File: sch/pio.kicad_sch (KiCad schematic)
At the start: 4 parts

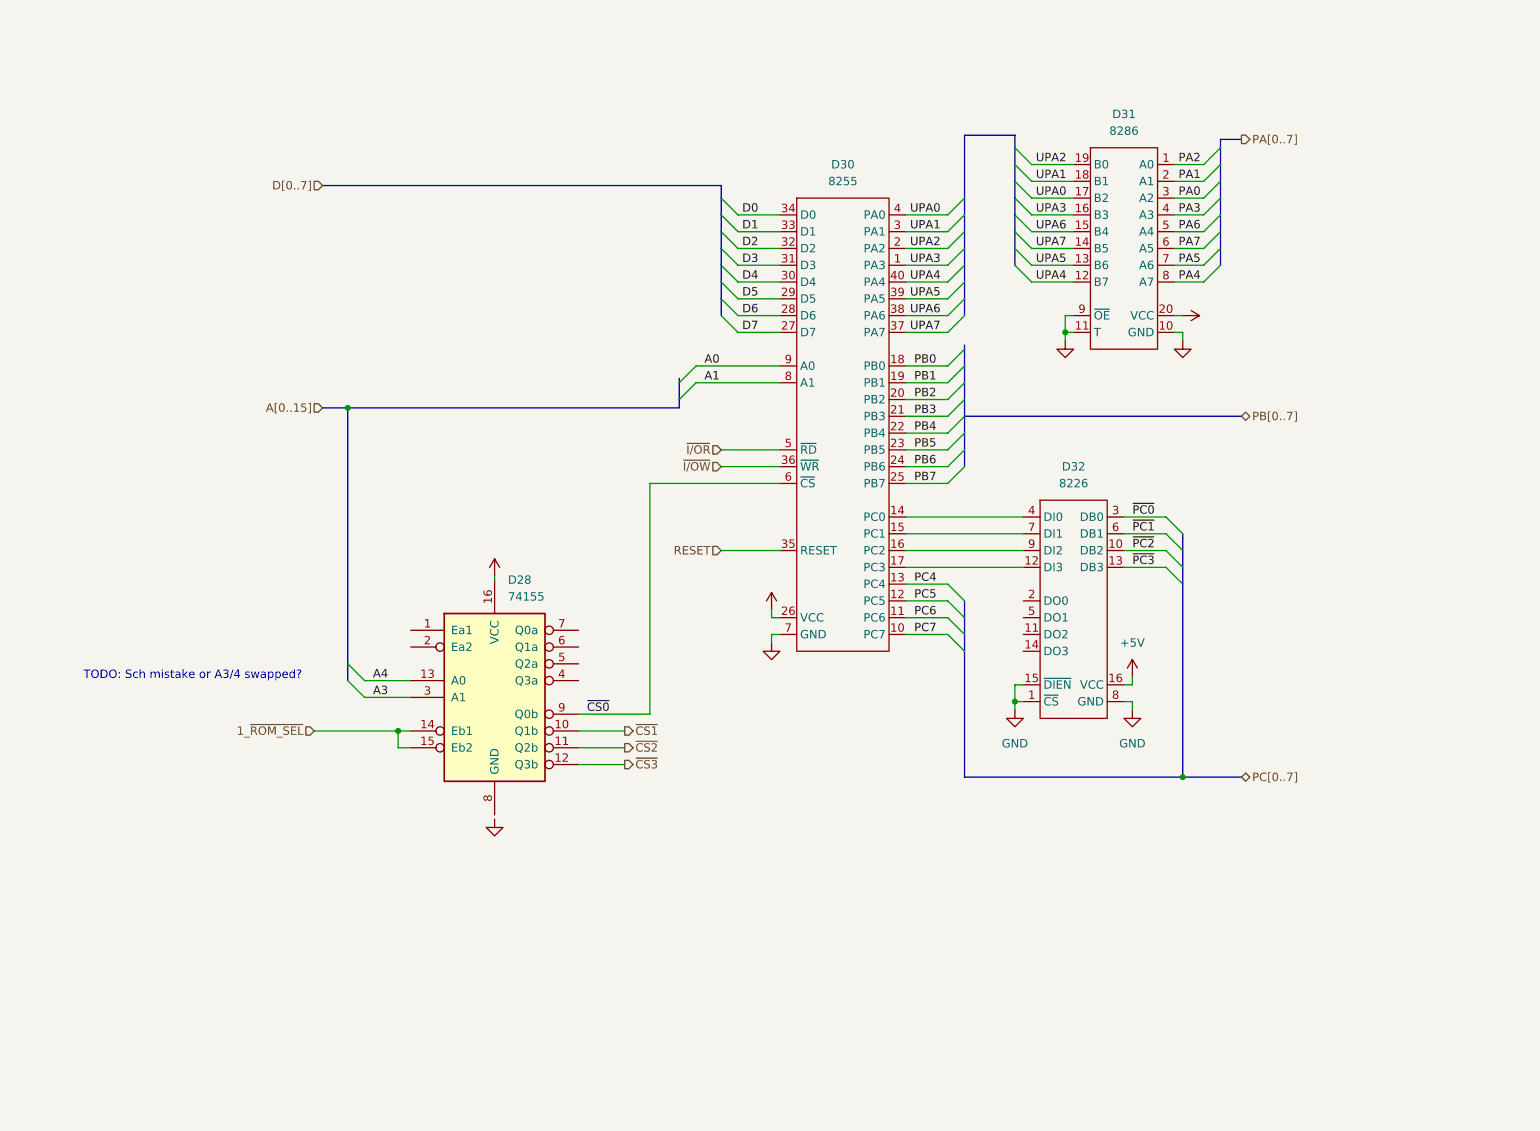
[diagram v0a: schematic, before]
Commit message: Sch: PIO part completed
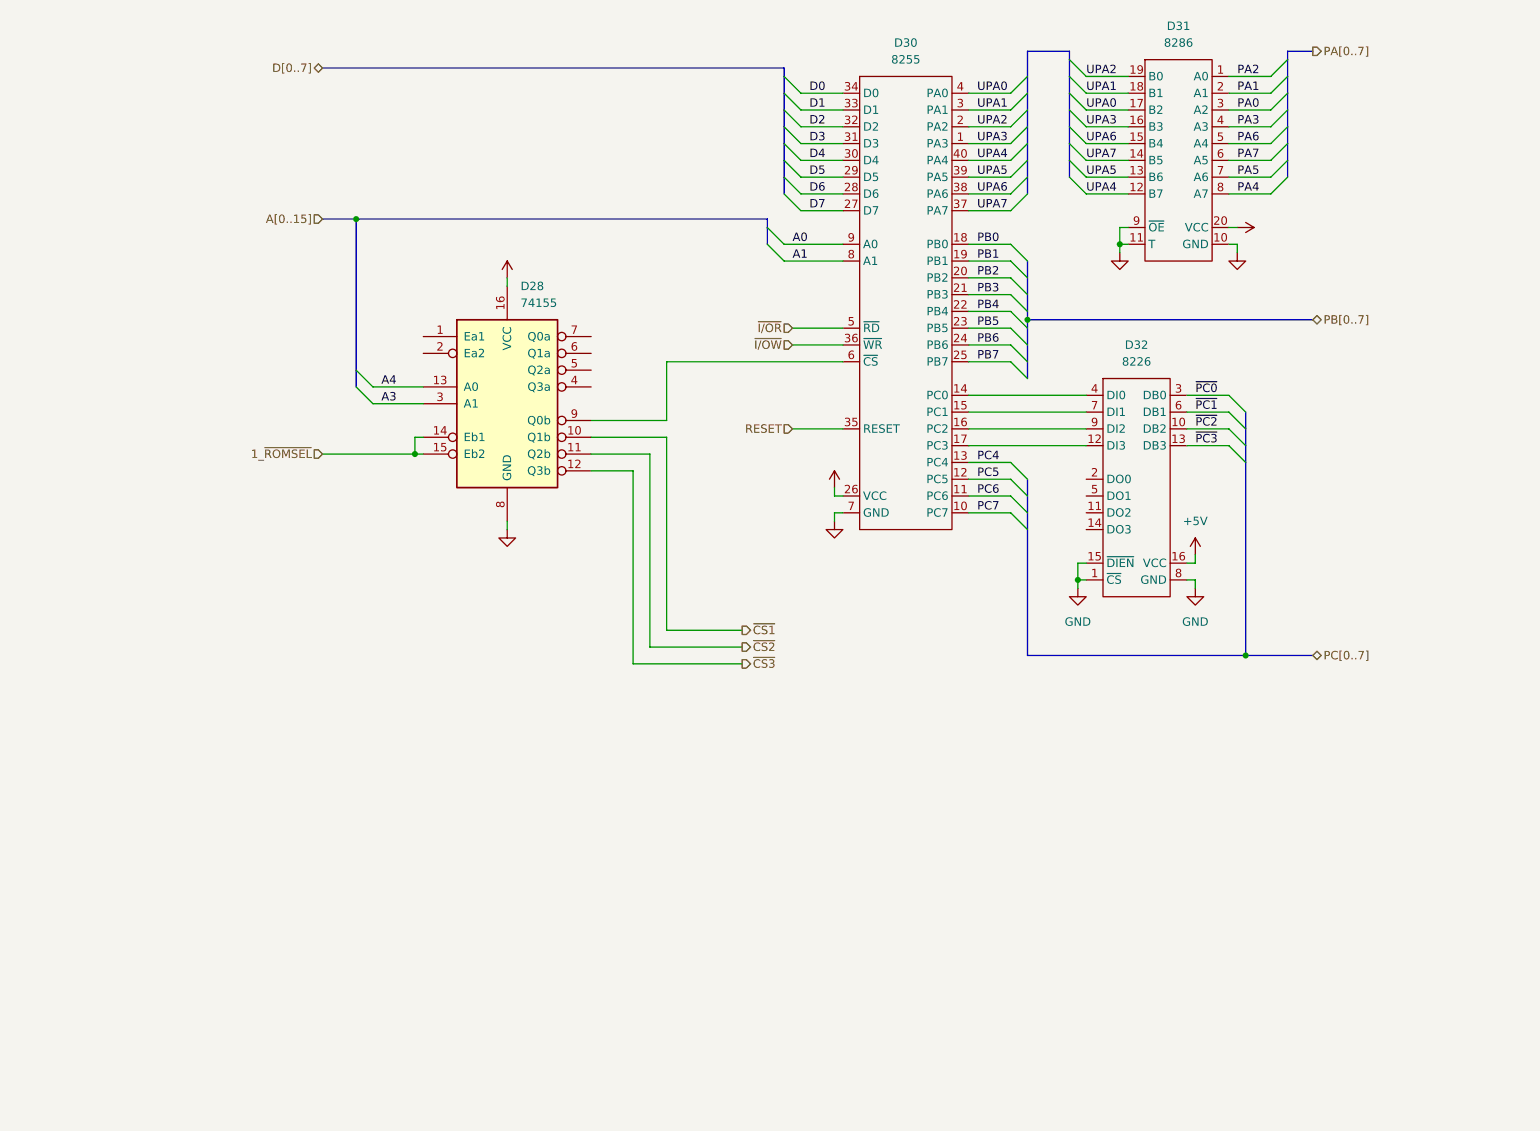
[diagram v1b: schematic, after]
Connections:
- net GND: now also D28.8 (GND)
- net 1_~{ROM_SEL} renamed 1_~{ROMSEL}
- net ~{CS0}: no longer names the net of D28.9 (Q0b), D30.6 (~{CS})
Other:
- note removed: "TODO: Sch mistake or A3/4 swapped?"
- moved on the sheet: D28, D30, D31, D32

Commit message: ch: PIO fixes
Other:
- note added: "WARNING: Address bus to be checked."
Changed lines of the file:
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@@
     (stroke (width 0) (type default) (color 0 0 0 0))
+  )
+  (text "WARNING: Address bus to be checked." (at 30.48 67.31 0)
+    (effects (font (size 1.27 1.27)) (justify left bottom))
   )
   (label "UPA6" (at 184.15 34.29 0)
@@
       (effects (font (size 1.27 1.27)) hide)
     )
-    (property "Value" "" (id 1) (at 146.05 82.55 0))
+    (property "Value" "+5V" (id 1) (at 146.05 82.55 0))
     (property "Footprint" "" (id 2) (at 146.05 86.36 0)
       (effects (font (size 1.27 1.27)) hide)
@@
       (effects (font (size 1.27 1.27)) hide)
     )
-    (property "Value" "" (id 1) (at 96.52 97.79 0))
+    (property "Value" "GND" (id 1) (at 96.52 97.79 0))
     (property "Footprint" "" (id 2) (at 96.52 92.71 0)
       (effects (font (size 1.27 1.27)) hide)
@@
       (effects (font (size 1.27 1.27)) hide)
     )
-    (property "Value" "" (id 1) (at 210.82 46.9899 90)
+    (property "Value" "+5V" (id 1) (at 210.82 46.9899 90)
       (effects (font (size 1.27 1.27)) (justify left))
     )
@@
       (effects (font (size 1.27 1.27)) hide)
     )
-    (property "Value" "" (id 1) (at 146.05 95.25 0))
+    (property "Value" "GND" (id 1) (at 146.05 95.25 0))
     (property "Footprint" "" (id 2) (at 146.05 91.44 0)
       (effects (font (size 1.27 1.27)) hide)
@@
       (effects (font (size 1.27 1.27)) hide)
     )
-    (property "Value" "" (id 1) (at 96.52 49.53 0))
+    (property "Value" "+5V" (id 1) (at 96.52 49.53 0))
     (property "Footprint" "" (id 2) (at 96.52 54.61 0)
       (effects (font (size 1.27 1.27)) hide)
@@
       (effects (font (size 1.27 1.27)) hide)
     )
-    (property "Value" "" (id 1) (at 207.01 54.61 0))
+    (property "Value" "GND" (id 1) (at 207.01 54.61 0))
     (property "Footprint" "" (id 2) (at 207.01 50.8 0)
       (effects (font (size 1.27 1.27)) hide)
@@
       (effects (font (size 1.27 1.27)) hide)
     )
-    (property "Value" "" (id 1) (at 189.23 54.61 0))
+    (property "Value" "GND" (id 1) (at 189.23 54.61 0))
     (property "Footprint" "" (id 2) (at 189.23 50.8 0)
       (effects (font (size 1.27 1.27)) hide)

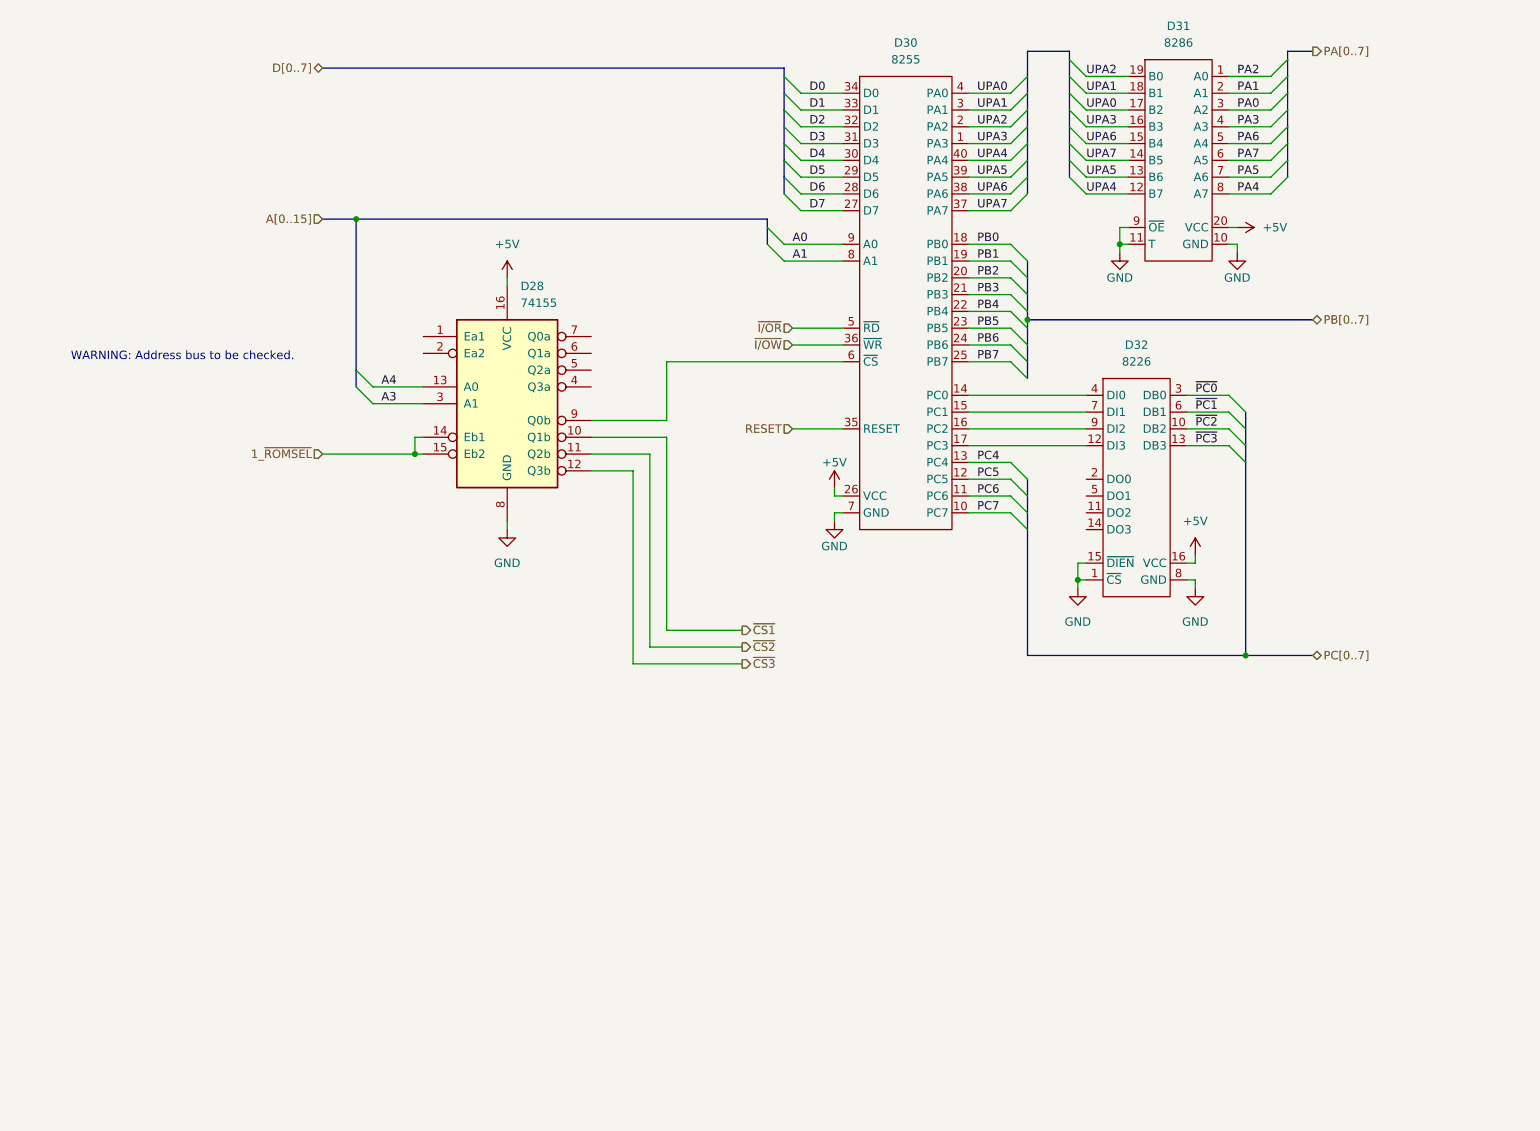
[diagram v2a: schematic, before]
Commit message: Sch: PIO block completed
Added X2 connector.
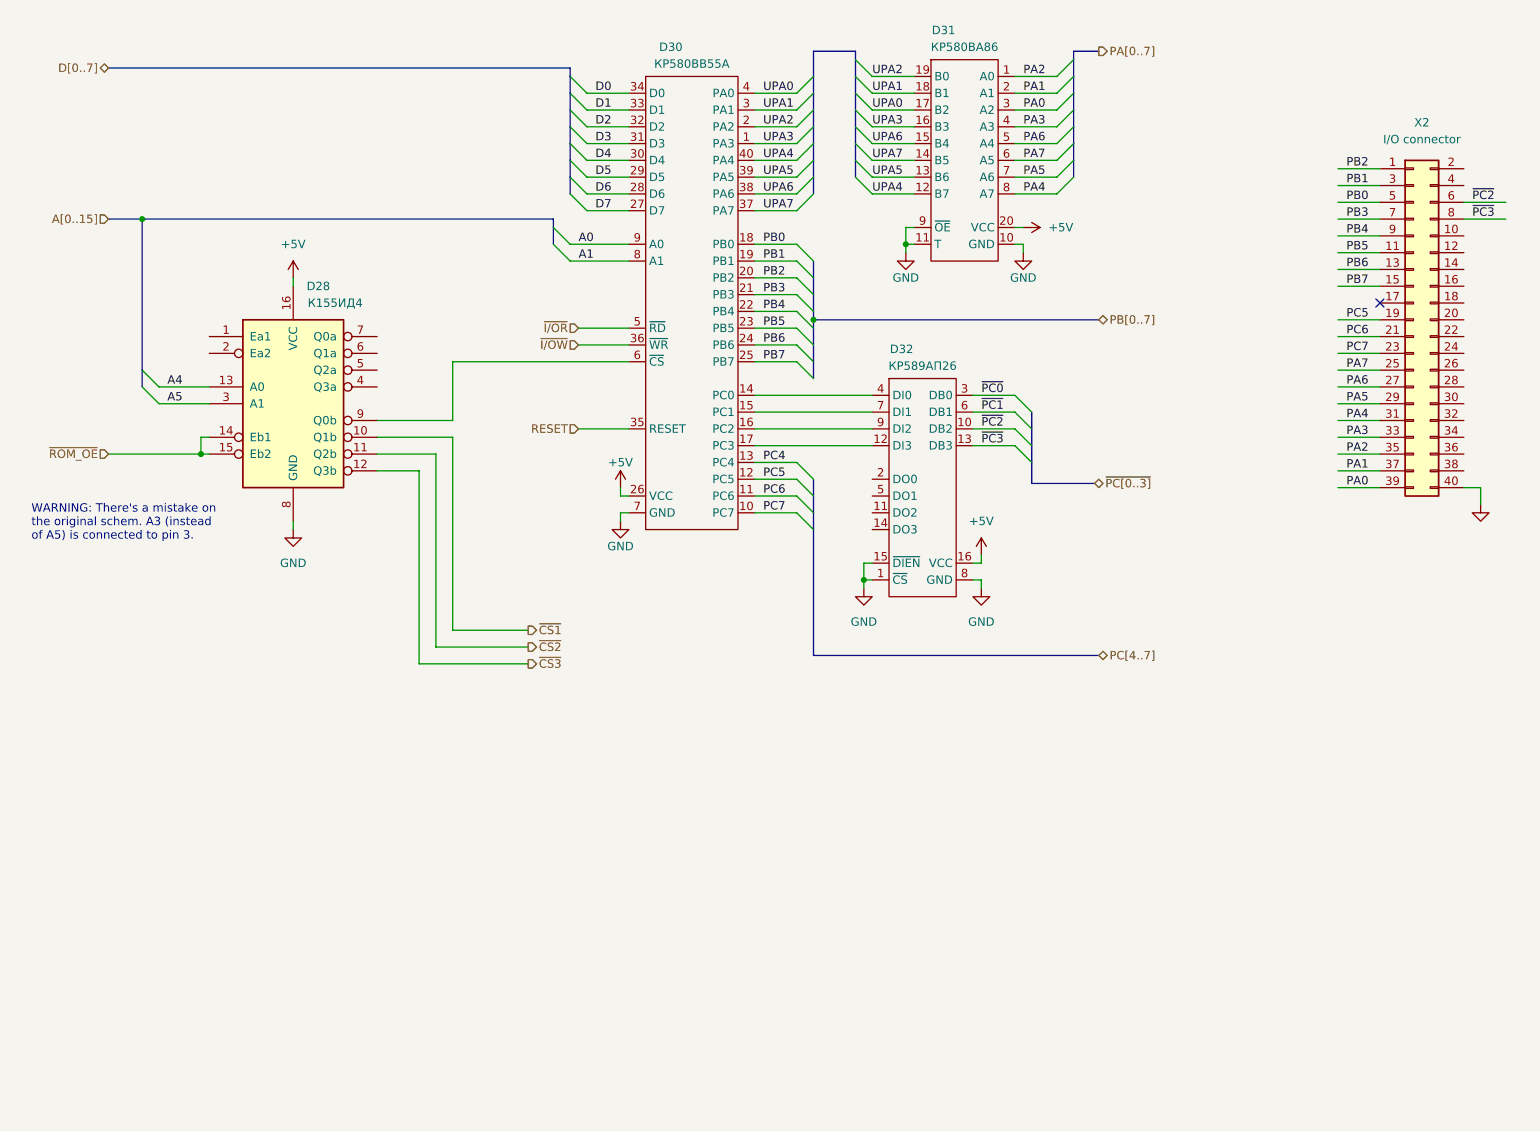
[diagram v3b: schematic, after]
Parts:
- added X2: I/O connector, symbol Connector_Generic:Conn_02x20_Odd_Even
- D28: value 74155 -> (none); CCCP (none) -> К155ИД4
- D30: value 8255 -> (none); CCCP (none) -> КР580ВВ55А
- D31: value 8286 -> (none); CCCP (none) -> КР580ВА86
- D32: value 8226 -> (none); CCCP (none) -> КР589АП26
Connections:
- net GND: now also X2.40 (Pin_40)
- net PA0: now also X2.39 (Pin_39)
- net PA1: now also X2.37 (Pin_37)
- net PA2: now also X2.35 (Pin_35)
- net PA3: now also X2.33 (Pin_33)
- net PA4: now also X2.31 (Pin_31)
- net PA5: now also X2.29 (Pin_29)
- net PA6: now also X2.27 (Pin_27)
- net PA7: now also X2.25 (Pin_25)
- net PB0: now also X2.5 (Pin_5)
- net PB1: now also X2.3 (Pin_3)
- net PB2: now also X2.1 (Pin_1)
- net PB3: now also X2.7 (Pin_7)
- net PB4: now also X2.9 (Pin_9)
- net PB5: now also X2.11 (Pin_11)
- net PB6: now also X2.13 (Pin_13)
- net PB7: now also X2.15 (Pin_15)
- net PC5: now also X2.19 (Pin_19)
- net PC6: now also X2.21 (Pin_21)
- net PC7: now also X2.23 (Pin_23)
- net ~{PC2}: now also X2.6 (Pin_6)
- net ~{PC3}: now also X2.8 (Pin_8)
- net 1_~{ROMSEL} renamed ~{ROM_OE}
- net A3 renamed A5
- no-connect marks 0 -> 1
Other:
- note added: "WARNING: There's a mistake on the original schem. A3 (instead of A5) is connected to pin 3."
- note removed: "WARNING: Address bus to be checked."
- moved on the sheet: D28, D30, D31, D32

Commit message: Schematics complete
Todo:
- part values
- full review
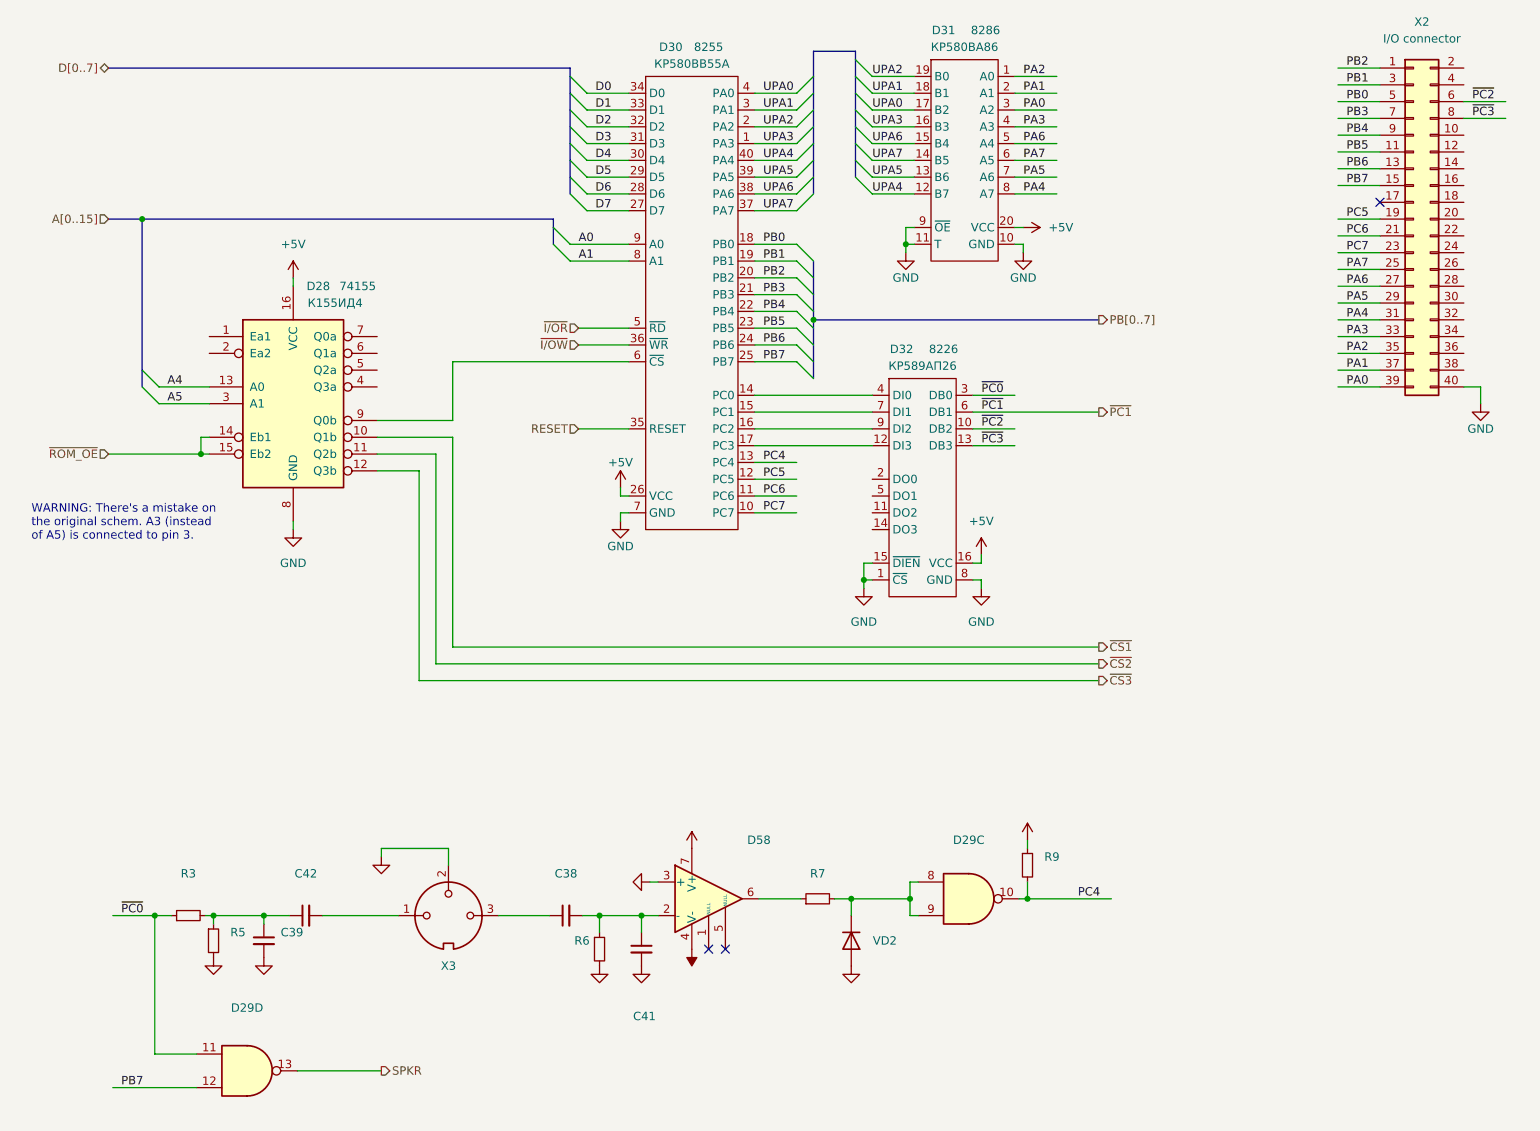
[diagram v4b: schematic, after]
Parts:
- added C38, C39, C41, C42: ~, symbol Device:C_Small
- added D29: (no value), symbol 74xx:74LS01
- added D58: ~, symbol Amplifier_Operational:LM741
- added R3, R5, R6, R7, R9: ~, symbol Device:R_Small
- added VD2: ~, symbol Diode:1N4148
- added X3: ~, symbol Connector:DIN-3
- D28: value (none) -> 74155
- D30: value (none) -> 8255
- D31: value (none) -> 8286
- D32: value (none) -> 8226
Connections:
- net +5V: now also D58.7 (V+), R9.1
- net GND: now also C39.2, C41.2, D58.3 (+), R5.2, R6.2, VD2.2 (A), X3.2
- net PB7: now also D29.12
- net PC4: now also D29.10, R9.2
- net ~{PC0}: now also D29.11, R3.1
- new net: C42.2, X3.1
- new net: C38.1, X3.3
- new net: C39.1, C42.1, R3.2, R5.1
- new net: D29.8, D29.9, R7.2, VD2.1 (K)
- new net: C38.2, C41.1, D58.2 (-), R6.1
- new net: D58.6, R7.1
- new net -5V: D58.4 (V-)
- new net SPKR: D29.13
- no-connect marks 1 -> 3
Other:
- moved on the sheet: X2
